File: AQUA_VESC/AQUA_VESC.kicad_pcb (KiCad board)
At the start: 2 copper layers, 101.6 x 77 mm, 219 parts, among them J1 Conn_01x06_Pin, J2 Conn_01x02_Pin, J3 Conn_01x05_Pin, M1 Motor_Servo_Hitec, Q1 TK3R2E06PL, Q10 AO3400A, Q11 AO3401A, Q12 AO3400A, Q13 AO3401A, Q2 TK3R2E06PL, Q3 TK3R2E06PL, Q4 TK3R2E06PL, Q5 TK3R2E06PL, Q6 TK3R2E06PL, Q7 AO3400A, Q8 AO3400A, Q9 AO3401A, U10 LMR16030SDDAR, U11 22uH, U13 TP2604-SR, U2 SMF05CT1G, U4 STM32F405RGTx, U5 TJA1051T-3, U6 TP2604-SR, U7 DRV8301QDCAQ1, U8 22uH, U9 AMS1117-3.3, X1 8MHz

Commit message: AQUA VESC仮完成
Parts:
- removed the C50 at (132.9, 54.2)
- removed the C57 at (132.9, 66.2)
- removed C69: 1n, Capacitor_SMD:C_0603_1608Metric
- removed IMU1: WHITE, LED_SMD:LED_0603_1608Metric
- removed the R1 at (89.1, 115.9)
- removed the U1 at (293.8, 142.4)
- removed UNUSED_GPIO1: Conn_02x04_Odd_Even, Connector_PinSocket_2.54mm:PinSocket_2x04_P2.54mm_Vertical
- added G***: LOGO, specific_footprint_library:aqua_rogo, B.Cu at (189.5, 75.0)
- added NT2: NetTie_2, NetTie:NetTie-2_SMD_Pad2.0mm, F.Cu at (190.8, 101.0)
- added NT3: NetTie_2, NetTie:NetTie-2_SMD_Pad0.5mm, F.Cu at (256.2, 88.8)
- added NT4: NetTie_2, NetTie:NetTie-2_SMD_Pad0.5mm, F.Cu at (194.8, 66.8)
- added NT5: NetTie_2, NetTie:NetTie-2_SMD_Pad0.5mm, F.Cu at (194.5, 65.2)
- added NT6: NetTie_2, NetTie:NetTie-2_SMD_Pad0.5mm, F.Cu at (213.8, 66.8)
- added NT7: NetTie_2, NetTie:NetTie-2_SMD_Pad0.5mm, F.Cu at (214.2, 65.2)
- added NT8: NetTie_2, NetTie:NetTie-2_SMD_Pad0.5mm, F.Cu at (238.8, 65.7)
- added NT9: NetTie_2, NetTie:NetTie-2_SMD_Pad0.5mm, F.Cu at (237.0, 65.3)
- C30: value 15n -> 10n
- C61: renamed from C63; value 0.1u -> 100n
- H5, H6, H7, H8, H9: footprint MountingHole:MountingHole_3.5mm_Pad -> MountingHole:MountingHole_3.5mm_Pad_Via
- J2, J3: moved to B.Cu
- SERVO_CNT1: value GREEN -> EMERALD
- U11: renamed from U12; value ~ -> MX27524ES
- U6: renamed from U7; footprint specific_footprint_library:DCA56_6P35X3P61 -> specific_footprint_library:HTSSOP-56_L14.0-W6.0-P0.50-LS8.0-BL
- U9: renamed from U10; footprint specific_footprint_library:DDA0008E_L -> Package_SO:SOIC-8-1EP_3.9x4.9mm_P1.27mm_EP2.41x3.3mm_ThermalVias
- USB1: value ~ -> Micro-B
- moved NT1 167.0 mm to (245.8, 88.0), turned to 90 degrees
- moved C1 131.8 mm to (220.2, 96.6), turned to 180 degrees
- moved R7 116.8 mm to (254.0, 104.5)
- moved R8 116.6 mm to (254.0, 103.0)
- moved J2 99.5 mm to (195.7, 120.0), turned to -90 degrees
- moved C60 29.9 mm to (179.0, 74.8), turned to -90 degrees
- moved R25 21.6 mm to (247.5, 92.0)
- moved C10 20.6 mm to (225.8, 91.0), turned to 90 degrees
- moved R15 19.9 mm to (250.5, 87.4)
- moved R17 19.6 mm to (252.8, 88.2)
- moved U5 19.4 mm to (251.2, 92.8)
- moved R31 18.6 mm to (249.5, 97.2), turned to 180 degrees
- moved R16 18.4 mm to (255.0, 91.0)
- moved R30 18.3 mm to (252.5, 97.2), turned to 180 degrees
- moved C17 18.1 mm to (255.0, 94.0)
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- renumbered C51 to C50, C52 to C51, C53 to C52, C54 to C53, C55 to C54, C56 to C55, C58 to C56, C59 to C57, C60 to C58, C61 to C59, C62 to C60, C64 to C62, C65 to C63, C66 to C64, C67 to C65, C68 to C66, C70 to C67, R2 to R1, R11 to R10, R12 to R11, R13 to R12, R14 to R13, R15 to R14, R16 to R15, R17 to R16, R18 to R17, R19 to R18, R20 to R19, R3 to R2, R21 to R20, R22 to R21, R23 to R22, R24 to R23, R25 to R24, R26 to R25, R27 to R26, R28 to R27, R29 to R28, R30 to R29, R4 to R3, R31 to R30, R32 to R31, R33 to R32, R34 to R33, R35 to R34, R36 to R35, R37 to R36, R38 to R37, R39 to R38, R40 to R39, R5 to R4, R41 to R40, R42 to R41, R43 to R42, R44 to R43, R45 to R44, R46 to R45, R47 to R46, R48 to R47, R49 to R48, R50 to R49, R6 to R5, R51 to R50, R52 to R51, R53 to R52, R54 to R53, R55 to R54, R56 to R55, R57 to R56, R58 to R57, R59 to R58, R60 to R59, R7 to R6, R61 to R60, R62 to R61, R63 to R62, R64 to R63, R65 to R64, R66 to R65, R67 to R66, R68 to R67, R69 to R68, R70 to R69, R8 to R7, R71 to R70, R72 to R71, R73 to R72, R74 to R73, R75 to R74, R76 to R75, R77 to R76, R78 to R77, R79 to R78, R80 to R79, R9 to R8, R81 to R80, R82 to R81, R83 to R82, R84 to R83, R85 to R84, R86 to R85, R87 to R86, R88 to R87, R89 to R88, R90 to R89, R10 to R9, U2 to U1, U11 to U10, U13 to U12, U3 to U2, U4 to U3, U5 to U4, U6 to U5, U8 to U7, U9 to U8
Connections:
- C16 pad 2: GNDPWR -> /DRV8301/SPC
- C31 pad 1: GNDPWR -> /DRV8301/SPA
- C32 pad 1: GNDPWR -> /DRV8301/SPB
- C48 pad 2: /DRV8301/H1_LOW -> Net-(Q2-S)
- C53 pad 2: /DRV8301/H2_LOW -> Net-(Q4-S)
- C57 pad 2: /DRV8301/H3_LOW -> Net-(Q6-S)
- Q2 pad 3: /DRV8301/H1_LOW -> Net-(Q2-S)
- Q4 pad 3: /DRV8301/H2_LOW -> Net-(Q4-S)
- Q6 pad 3: /DRV8301/H3_LOW -> Net-(Q6-S)
- R15 pad 1: GNDPWR -> /DRV8301/SPC
- R42 pad 2: /DRV8301/H1_LOW -> Net-(Q2-S)
- R44 pad 2: /DRV8301/H1_LOW -> Net-(Q2-S)
- R45 pad 2: /DRV8301/H1_LOW -> Net-(Q2-S)
- R52 pad 2: /DRV8301/H2_LOW -> Net-(Q4-S)
- R54 pad 2: /DRV8301/H2_LOW -> Net-(Q4-S)
- R55 pad 2: /DRV8301/H2_LOW -> Net-(Q4-S)
- R62 pad 2: /DRV8301/H3_LOW -> Net-(Q6-S)
- R64 pad 2: /DRV8301/H3_LOW -> Net-(Q6-S)
- R66 pad 2: /DRV8301/H3_LOW -> Net-(Q6-S)
- U6 pad 30: GNDPWR -> /DRV8301/SPB
- U6 pad 32: GNDPWR -> /DRV8301/SPA
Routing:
- net +3V3: track 158.6 -> 74.4 mm, vias 13 -> 36
- net +5V: track 134.8 -> 207.1 mm, vias 7 -> 9
- net /DRV8301/SPA: track 0.00 -> 46.8 mm, vias 0 -> 2
- net /DRV8301/SENS1: track 1.71 -> 37.0 mm, vias 0 -> 2
- net /DRV8301/SPC: track 0.00 -> 34.7 mm, vias 0 -> 2
- net /STM32F405/USB_DP: track 0.00 -> 32.1 mm, vias 0 -> 2
- net /STM32F405/USB_DM: track 0.00 -> 31.8 mm, vias 0 -> 2
- net /DRV8301/SPB: track 0.00 -> 31.3 mm, vias 0 -> 2
- net SWCLK: track 0.00 -> 31.0 mm
- net /DRV8301/H3_LOW: track 55.0 -> 84.4 mm, vias 12 -> 6
- net GNDPWR: track 5.73 -> 32.8 mm, vias 0 -> 126
- net /DRV8301/BR_SO2: track 3.50 -> 25.6 mm
- net /DRV8301/BR_SO3: track 1.65 -> 23.6 mm, vias 0 -> 2
- net /STM32F405/AN_IN: track 0.00 -> 20.7 mm, vias 0 -> 2
- net /DRV8301/SENS3: track 1.63 -> 21.4 mm, vias 0 -> 2
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- added copper zone on B.Cu, net +3V3
- added copper zone on B.Cu, net /Power MOSFETs/TEMP
- added copper zone on F.Cu, net /Power MOSFETs/TEMP
- added copper zone on B.Cu, net GNDPWR
- added copper zone on B.Cu, net Net-(Q2-S)
- added copper zone on F.Cu, net Net-(Q2-S)
- added copper zone on B.Cu, net Net-(Q4-S)
- added copper zone on F.Cu, net Net-(Q4-S)
- added copper zone on B.Cu, net Net-(Q6-S)
- added copper zone on F.Cu, net Net-(Q6-S)
- removed copper zone on B.Cu, net /DRV8301/H1_LOW
- removed copper zone on F.Cu, net /DRV8301/H1_LOW
- removed copper zone on B.Cu, net /DRV8301/H2_LOW
- removed copper zone on F.Cu, net /DRV8301/H2_LOW
- removed copper zone on B.Cu, net /DRV8301/H3_LOW
- removed copper zone on F.Cu, net /DRV8301/H3_LOW
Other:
- board size 101.6 x 77 mm -> 101.5 x 77.8 mm
- board text added: "+"
- board text added: "-"
- board text added: "3V3"
- board text added: "7V"
- board text added: "Azimuth Thruster Driver (based on Cheap FOCer2)"
- board text added: "B R G"
- board text added: "CAN R"
- board text added: "C_BST"
- board text added: "Compatible with VESC® Software"
- board text added: "FAULT"
- board text added: "G R B"
- board text added: "GND"
- board text added: "H"
- board text added: "H L"
- board text added: "MCU"
- board text added: "NRST"
- board text added: "PWM"
- board text added: "REV00"
- board text added: "RGBLED"
- board text added: "R_DTC"
- board text added: "R_GH_A"
- board text added: "R_GH_B"
- board text added: "R_GH_C"
- board text added: "R_GL_A"
- board text added: "R_GL_B"
- board text added: "R_GL_C"
- board text added: "SERVO"
- board text added: "ST-LINK"
- board text added: "SWCLK"
- board text added: "SWDIO"
- board text added: "VESC_ID"
- board text added: "Voltage_IN"
- board text added: "Water sensor"
- board text added: "servo gpio-icu PB6 RED gpio-tx PB10 GREEN gpio-rx PB11 BLUE gpio-adc2 ADC5 water sensor gpio-adc ADC6"
- board text added: "test type"

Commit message: VESC発注
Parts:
- moved USB1 130.3 mm to (131.5, 72.5)
- moved 5V1 130.3 mm to (71.0, 74.2)
- moved C10 130.3 mm to (99.2, 59.8)
- moved C11 130.3 mm to (96.5, 75.0)
- moved C12 130.3 mm to (109.0, 75.2)
- moved C13 130.3 mm to (112.5, 66.0)
- moved C14 130.3 mm to (112.5, 64.5)
- moved C15 130.3 mm to (127.5, 83.3)
- moved C16 130.3 mm to (113.8, 34.2)
- moved C17 130.3 mm to (128.5, 62.8)
- moved C18 130.3 mm to (80.0, 74.8)
- moved C19 130.3 mm to (82.0, 74.8)
- moved C2 130.3 mm to (113.0, 76.0)
- moved C20 130.3 mm to (70.0, 69.2)
- moved C21 130.3 mm to (90.2, 70.0)
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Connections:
- RGBLED1 pad 1: /RGBLED_Driver/BLUE_OUT -> GNDPWR
- RGBLED1 pad 2: /RGBLED_Driver/RED_OUT -> /RGBLED_Driver/BLUE_OUT
- RGBLED1 pad 3: /RGBLED_Driver/GREEN_OUT -> /RGBLED_Driver/RED_OUT
- RGBLED1 pad 4: GNDPWR -> /RGBLED_Driver/GREEN_OUT
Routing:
- net +3V3: track 74.4 -> 71.0 mm
- net +5V: track 207.1 -> 203.9 mm
- net /RGBLED_Driver/RED_GATE: track 44.5 -> 46.6 mm
- net /RGBLED_Driver/GREEN_GATE: track 49.1 -> 50.9 mm
- net /RGBLED_Driver/BLUE_GATE: track 37.5 -> 38.7 mm
- net Net-(Q12-D): track 9.11 -> 9.68 mm
- net Net-(Q8-D): track 8.32 -> 8.85 mm
- net GNDPWR: vias 126 -> 125

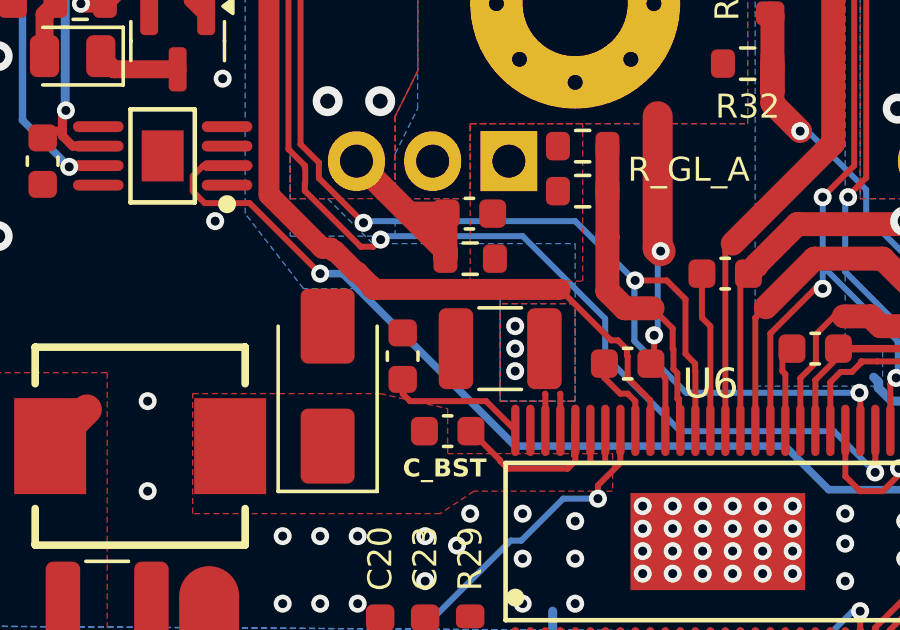
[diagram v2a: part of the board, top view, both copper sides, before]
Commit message: スラスタLED基盤　REV02作成
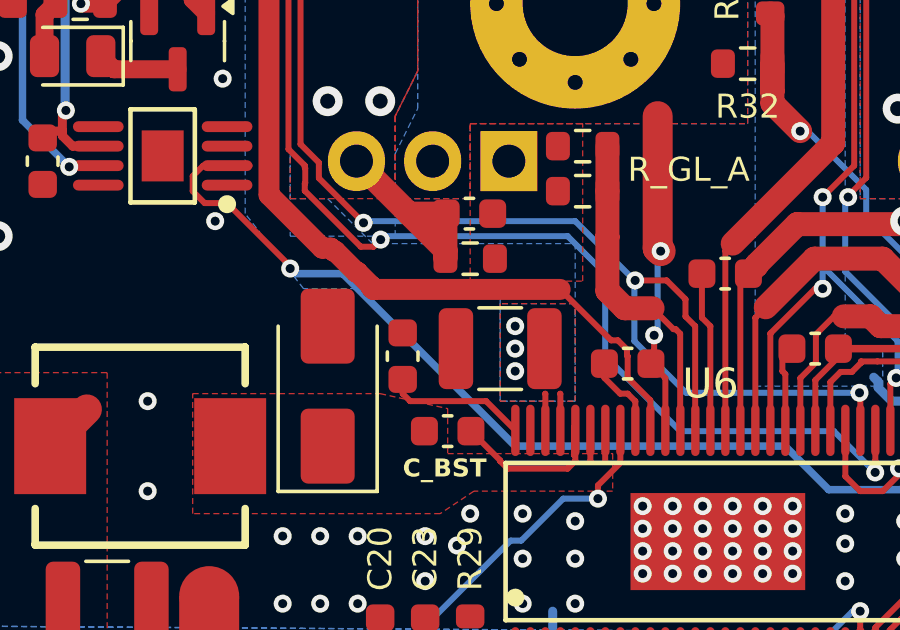
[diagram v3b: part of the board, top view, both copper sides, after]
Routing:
- net /DRV8301/SPA: track 46.8 -> 47.7 mm
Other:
- board text added: "REV01"
- board text removed: "REV00"
- board text removed: "test type"

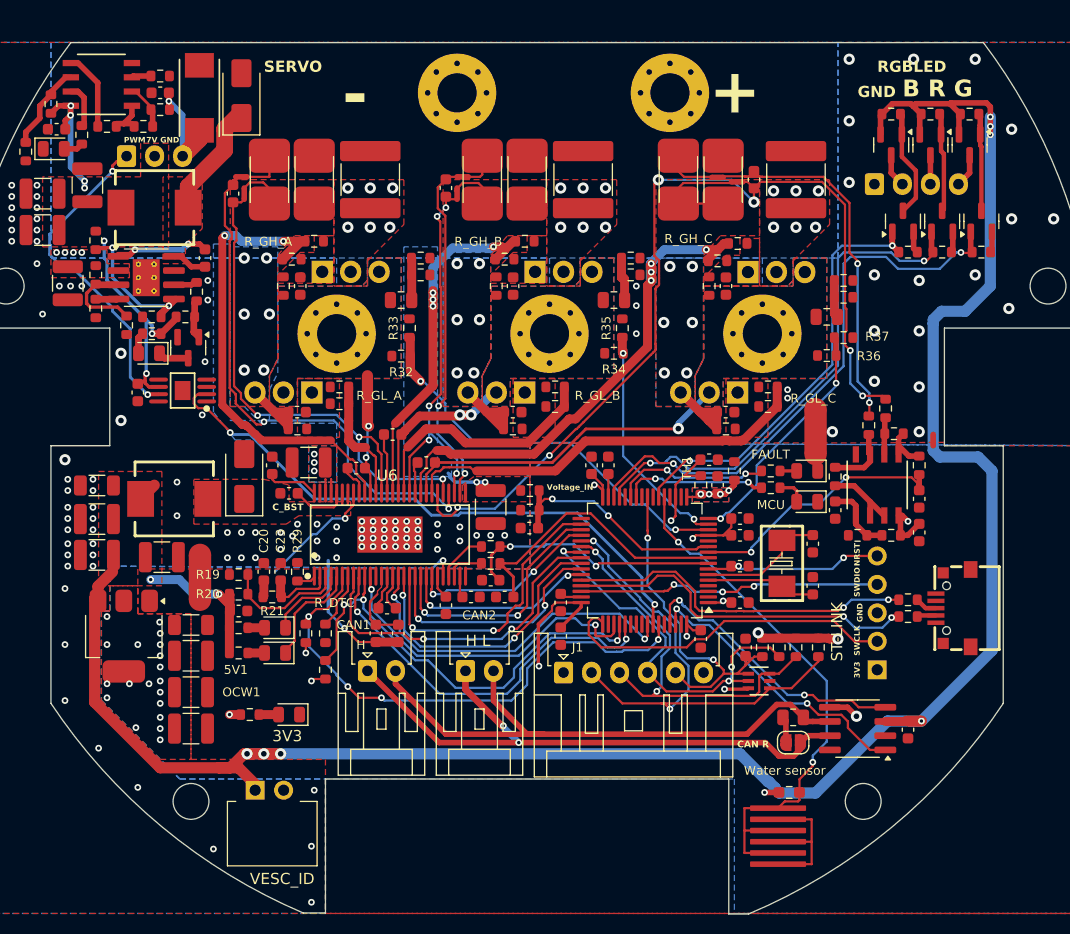
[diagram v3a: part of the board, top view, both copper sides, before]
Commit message: AQUA_VESC REV01作成
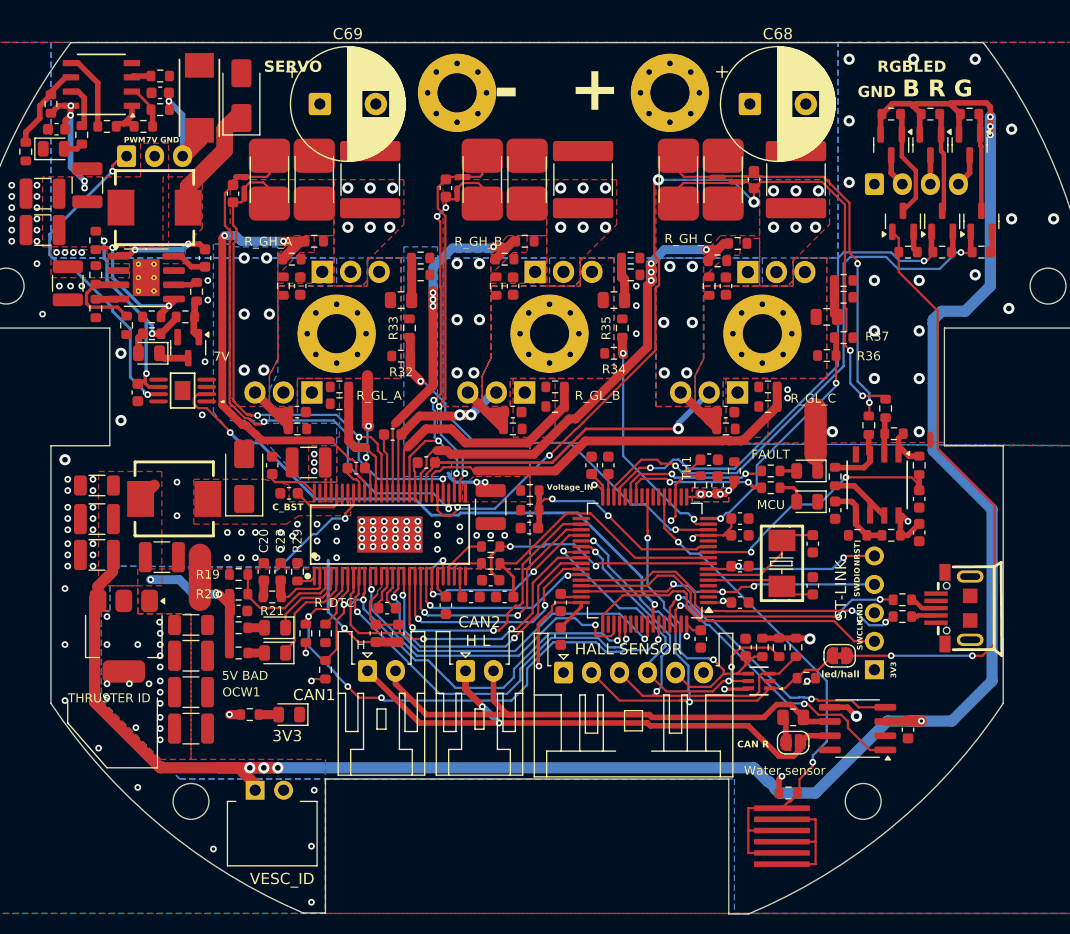
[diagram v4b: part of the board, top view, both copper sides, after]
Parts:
- added C68: 330u, Capacitor_THT:CP_Radial_D10.0mm_P5.00mm, F.Cu at (113.4, 27.5)
- added C69: 330u, Capacitor_THT:CP_Radial_D10.0mm_P5.00mm, F.Cu at (75.0, 27.5)
- added JP2: SolderJumper_2_Bridged, Jumper:SolderJumper-2_P1.3mm_Bridged_RoundedPad1.0x1.5mm, F.Cu at (121.4, 76.8)
- C47, C48, C52, C53, C56, C57: value 1n -> 10n
- CAN1, CAN2: footprint Connector_JST:JST_XA_S02B-XASK-1N-BN_1x02_P2.50mm_Horizontal -> Connector_JST:JST_XA_S02B-XASK-1_1x02_P2.50mm_Horizontal
- D3: value YELLOW -> EMERALD
- J1: footprint Connector_JST:JST_XA_S06B-XASK-1N-BN_1x06_P2.50mm_Horizontal -> Connector_JST:JST_XA_S06B-XASK-1_1x06_P2.50mm_Horizontal
- R10: footprint Resistor_SMD:R_0603_1608Metric_Pad0.98x0.95mm_HandSolder -> Resistor_SMD:R_0603_1608Metric
- R20: value 10k -> 18k
- R81: value 120k -> 200k
- USB1: value Micro-B -> ~; footprint specific_footprint_library:MICRO-USB-SMD_MICRO-QTZB5.5 -> specific_footprint_library:MICRO-USB-SMD_5P-P0.65-H-F_MICRO5.9MMUSB
- moved R3 2.95 mm to (118.4, 78.8), turned to 180 degrees
- moved R7 0.50 mm to (127.0, 73.2)
- moved R8 0.50 mm to (127.0, 71.8)
- moved U2 0.35 mm to (116.2, 96.8)
- moved J3 0.25 mm to (124.5, 78.0)
- moved NT3 0.25 mm to (129.5, 57.5)
- moved R10 0.09 mm to (116.8, 89.0), turned to 180 degrees
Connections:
- Q12 pad 1: /RGBLED_Driver/BLUE_GATE -> BLUE_GATE
- R10 pad 1: +3V3 -> /STM32F405/ADC_EXT
- R10 pad 2: /STM32F405/ADC_EXT -> +3V3
- R7 pad 1: /STM32F405/USB_DP -> /STM32F405/USB_DM
- R8 pad 1: /STM32F405/USB_DM -> /STM32F405/USB_DP
- R88 pad 1: /RGBLED_Driver/BLUE_GATE -> BLUE_GATE
- U3 pad 22: /RGBLED_Driver/BLUE_GATE -> ADC_EXT2
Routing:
- net BLUE_GATE: track 0.00 -> 54.2 mm, vias 0 -> 2
- net /RGBLED_Driver/BLUE_GATE: track 38.7 -> 0.00 mm, vias 2 -> 0
- net Net-(Q6-S): track 19.1 -> 15.1 mm
- net /CAN/CANL: track 52.4 -> 48.7 mm
- net /CAN/CANH: track 54.0 -> 51.5 mm
- net SWCLK: track 31.0 -> 28.5 mm
- net +5V: track 203.9 -> 201.9 mm
- net +3V3: track 71.0 -> 69.2 mm
- net /STM32F405/ADC_EXT: track 36.8 -> 36.0 mm
- net /STM32F405/USB_DP: track 32.1 -> 31.4 mm
- net /DRV8301/H1_LOW: track 48.9 -> 49.4 mm
- net /STM32F405/USB_DM: track 31.8 -> 31.3 mm
- net NRST: track 15.5 -> 15.0 mm
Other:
- board text added: "(based on Cheap FOCer2)"
- board text added: "5V BAD"
- board text added: "Azimuth Thruster Driver"
- board text added: "HALL SENSOR"
- board text added: "THRUSTER ID"
- board text added: "led/hall"
- board text added: "servo gpio-icu PB6 RED gpio-tx PB10 GREEN gpio-rx PB11 BLUE gpio-hall1 PC6 water sensor gpio-adc ADC6"
- board text removed: "Azimuth Thruster Driver (based on Cheap FOCer2)"
- board text removed: "servo gpio-icu PB6 RED gpio-tx PB10 GREEN gpio-rx PB11 BLUE gpio-adc2 ADC5 water sensor gpio-adc ADC6"
